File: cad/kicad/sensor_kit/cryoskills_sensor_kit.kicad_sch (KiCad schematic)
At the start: 12 parts, among them J1 PWR_SENSE_Panel, J2 PWR_SENSE_Battery, J3 PWR_In, U1 LM317_TO-220

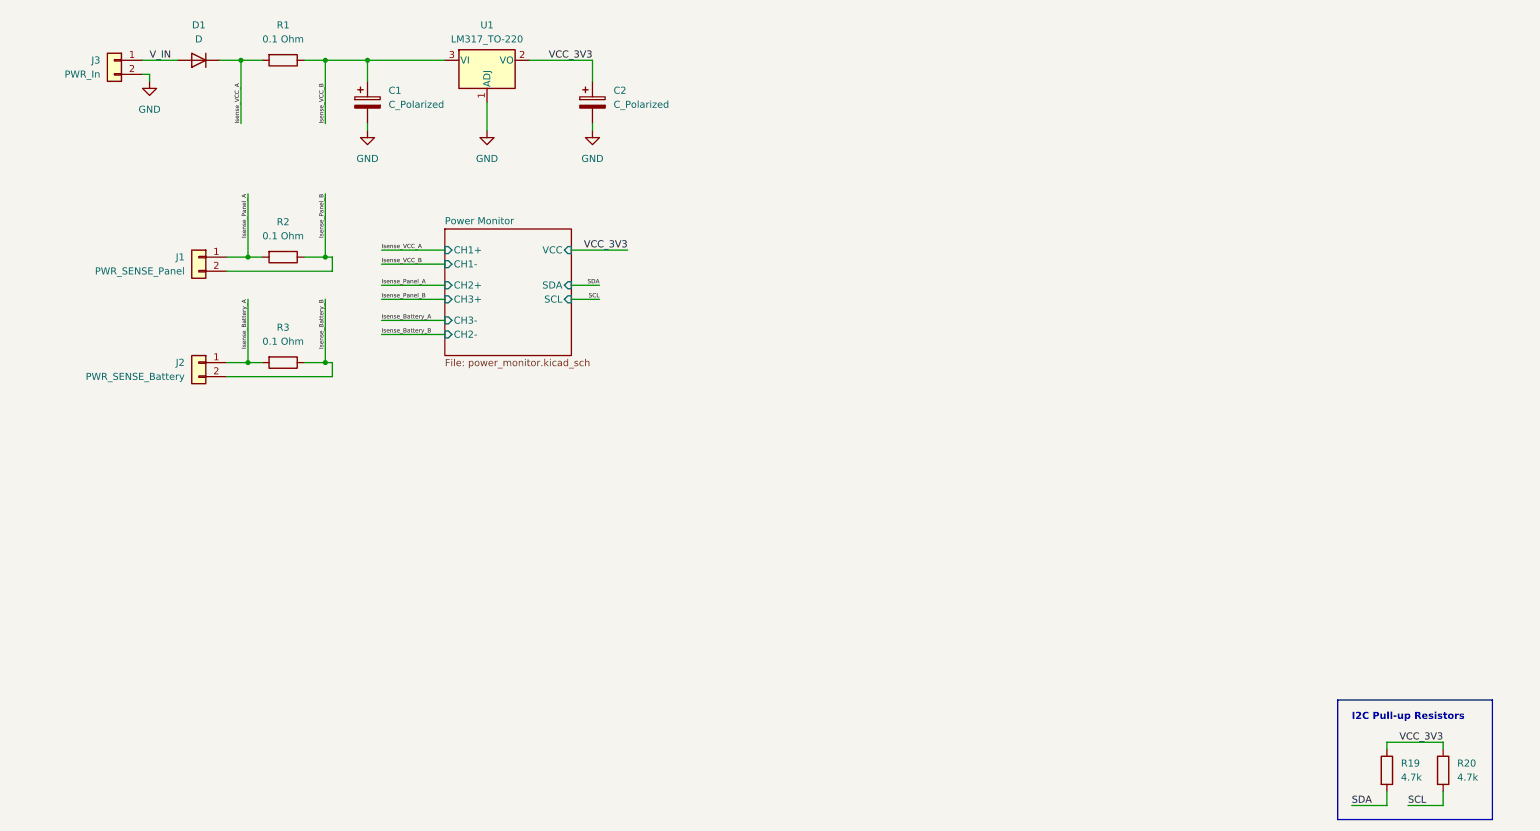
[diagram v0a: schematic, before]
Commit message: moves sensors to new board and adds discussion around ADS1120 based analog temp sensor to design notes.
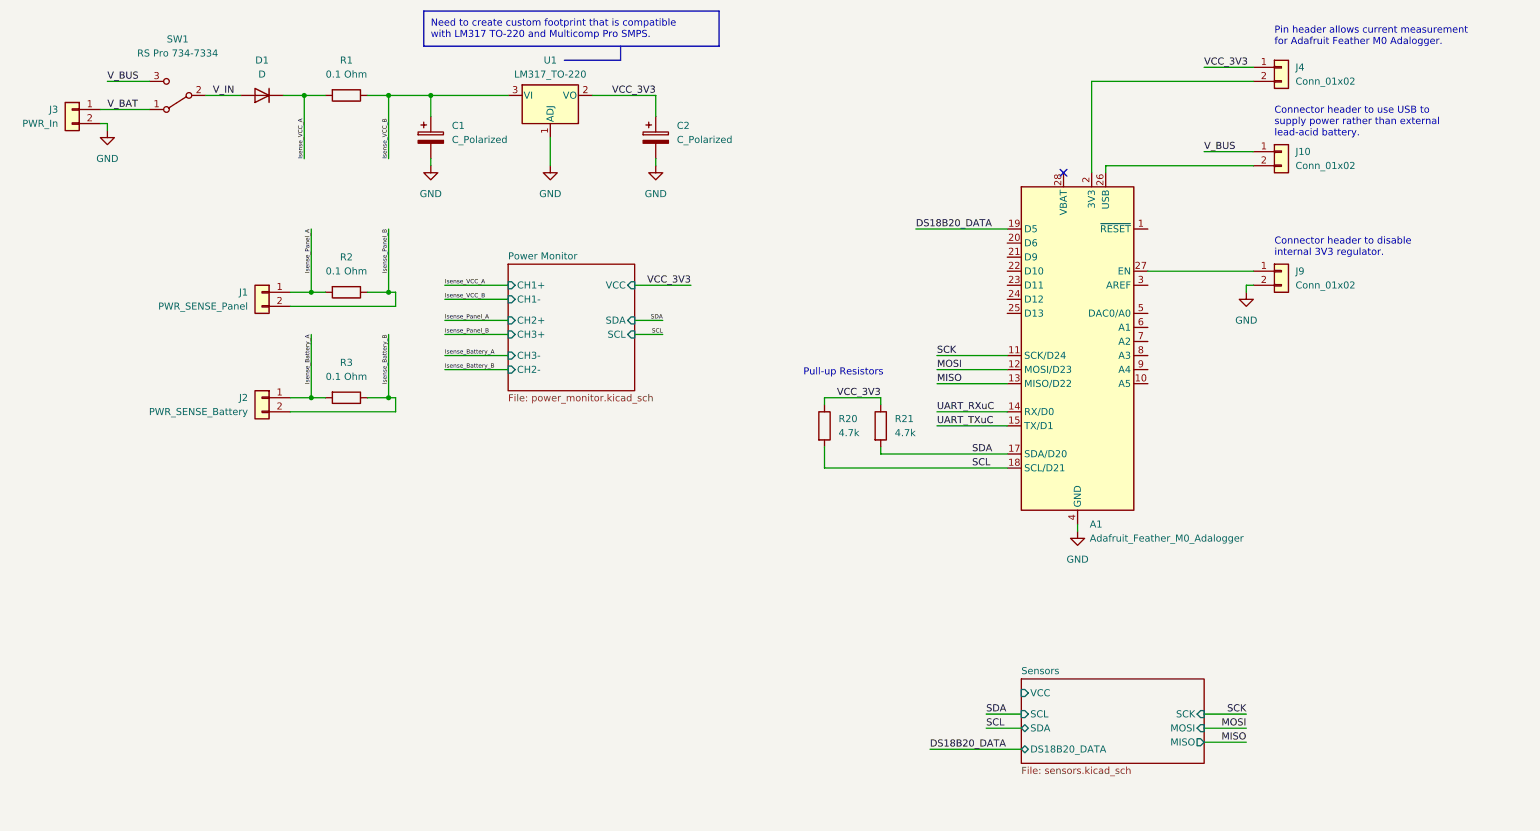
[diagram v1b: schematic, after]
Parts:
- removed R19: 4.7k, symbol Device:R
- added A1: Adafruit_Feather_M0_Adalogger, Module:Adafruit_Feather, symbol MCU_Module:Adafruit_Feather_M0_Adalogger
- added J10, J4, J9: Conn_01x02, Connector_PinHeader_2.54mm:PinHeader_1x02_P2.54mm_Vertical, symbol Connector_Generic:Conn_01x02
- added R21: 4.7k, symbol Device:R
- added SW1: RS Pro 734-7334, cryoskills_sensor_kit:RSPRO_7347334_SWSlide_SPDT, symbol Switch:SW_SPDT
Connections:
- net GND: now also A1.16 (GND), A1.4 (GND), J9.2 (Pin_2)
- net SCL: now also A1.18 (SCL/D21)
- net SDA: now also A1.17 (SDA/D20), R21.2
- net VCC_3V3: now also J4.1 (Pin_1), R21.1
- net V_IN: now also SW1.2 (B); no longer J3.1 (Pin_1)
- new net: A1.26 (USB), J10.2 (Pin_2)
- new net: A1.2 (3V3), J4.2 (Pin_2)
- new net: A1.27 (EN), J9.1 (Pin_1)
- new net DS18B20_DATA: A1.19 (D5)
- new net MISO: A1.13 (MISO/D22)
- new net MOSI: A1.12 (MOSI/D23)
- new net SCK: A1.11 (SCK/D24)
- new net UART_RXuC: A1.14 (RX/D0)
- new net UART_TXuC: A1.15 (TX/D1)
- new net V_BAT: J3.1 (Pin_1), SW1.1 (A)
- new net V_BUS: J10.1 (Pin_1), SW1.3 (C)
- no-connect marks 0 -> 1
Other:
- added sheet Sensors (sensors.kicad_sch)
- note added: "Connector header to disable internal 3V3 regulator."
- note added: "Connector header to use USB to supply power rather than external lead-acid battery."
- note added: "Need to create custom footprint that is compatible with LM317 TO-220 and Multicomp Pro SMPS."
- note added: "Pin header allows current measurement for Adafruit Feather M0 Adalogger."
- note added: "Pull-up Resistors"
- note removed: "I2C Pull-up Resistors"
- company: (none) -> Cardiff University
- title: (none) -> CryoSkills Sensor Kit
- moved on the sheet: C1, C2, D1, J1, J2, J3, R1, R2, R3, U1

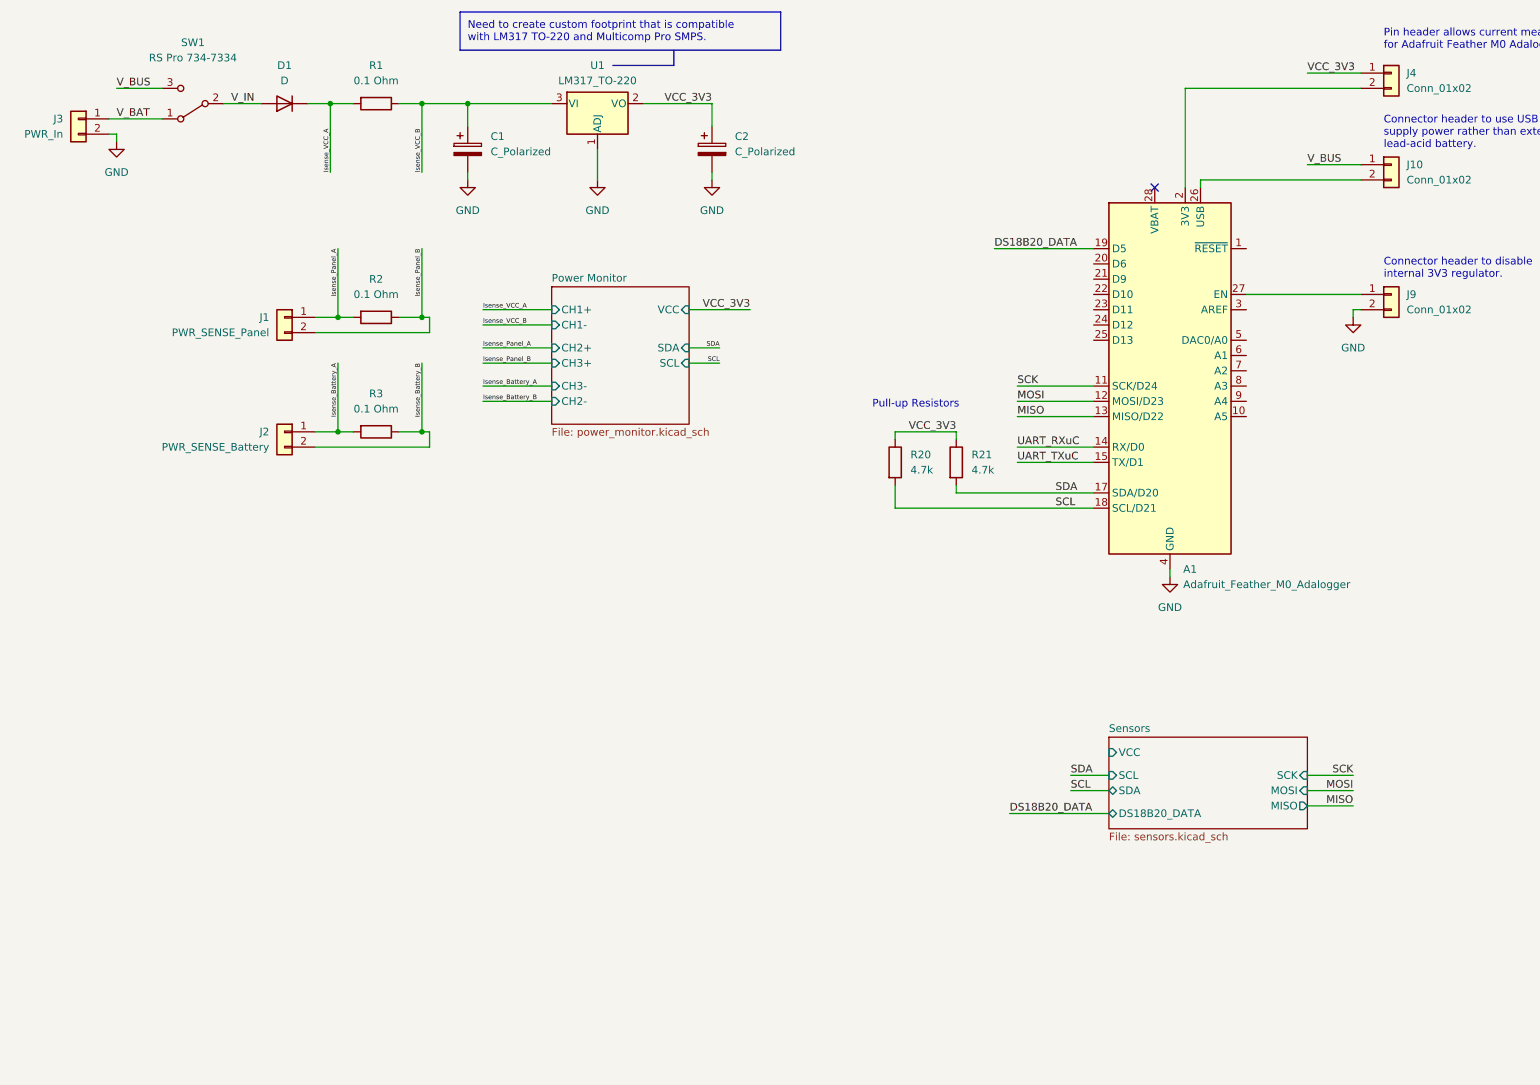
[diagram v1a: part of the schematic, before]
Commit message: adds further sensors to board layout
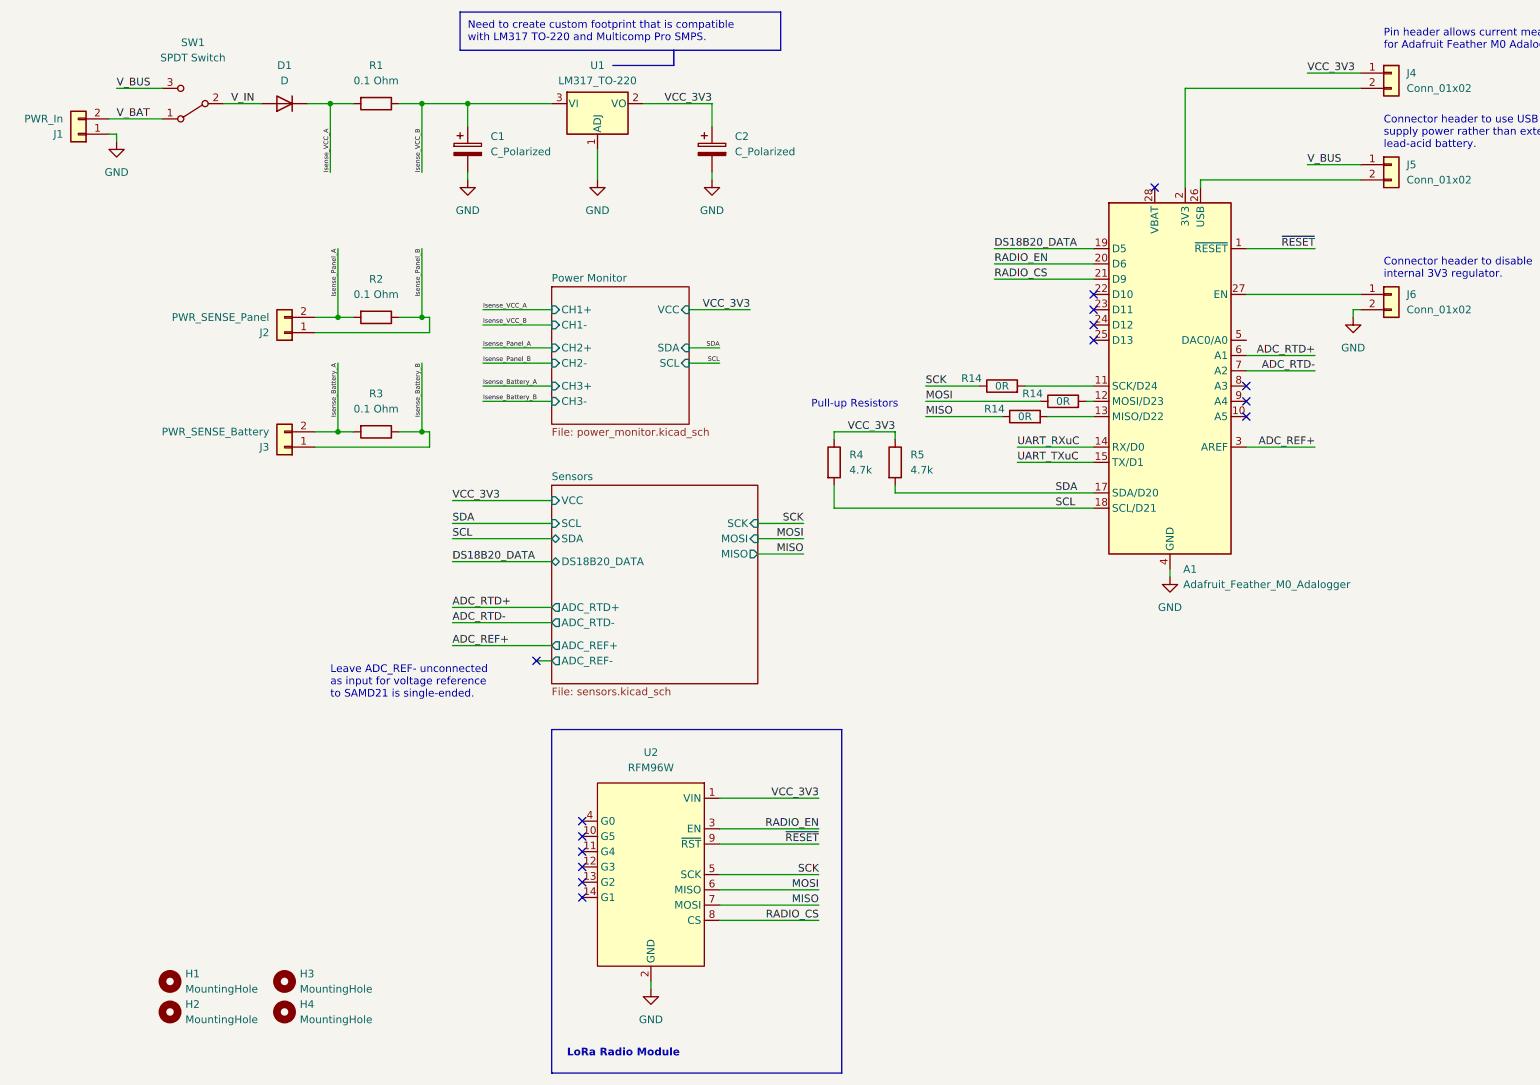
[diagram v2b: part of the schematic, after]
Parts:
- added H1, H2, H3, H4: MountingHole, MountingHole:MountingHole_3.2mm_M3, symbol Mechanical:MountingHole
- added R14 (x3): 0R, Resistor_SMD:R_0805_2012Metric_Pad1.20x1.40mm_HandSolder, symbol Device:R
- added U2: RFM96W, cryoskills_sensor_kit:RFM96W, symbol cryoskills_sensor_kit:RFM96W
- A1: Manufacturer (none) -> Adafruit; MftrPartNo (none) -> 2796; Supplier (none) -> RS Components; SupplierPartNo (none) -> 124-5517
- D1: footprint (none) -> Diode_SMD:D_SMB
- J1: renamed from J3; footprint (none) -> cryoskills_sensor_kit:TerminalBlock_Multicomp_5.08_2way_MP012059; Manufacturer (none) -> Multicomp PRO; MftrPartNo (none) -> MP12059; Supplier (none) -> Farnell; SupplierPartNo (none) -> 4179098
- J2: renamed from J1; footprint (none) -> cryoskills_sensor_kit:TerminalBlock_Multicomp_5.08_2way_MP012059; Manufacturer (none) -> Multicomp PRO; MftrPartNo (none) -> MP12059; Supplier (none) -> Farnell; SupplierPartNo (none) -> 4179098
- J3: renamed from J2; footprint (none) -> cryoskills_sensor_kit:TerminalBlock_Multicomp_5.08_2way_MP012059; Manufacturer (none) -> Multicomp PRO; MftrPartNo (none) -> MP12059; Supplier (none) -> Farnell; SupplierPartNo (none) -> 4179098
- R1, R2, R3: footprint (none) -> Resistor_SMD:R_1206_3216Metric
- R4: renamed from R20; footprint (none) -> Resistor_SMD:R_0805_2012Metric_Pad1.20x1.40mm_HandSolder
- R5: renamed from R21; footprint (none) -> Resistor_SMD:R_0805_2012Metric_Pad1.20x1.40mm_HandSolder
- SW1: value RS Pro 734-7334 -> SPDT Switch; Manufacturer (none) -> RS Pro; MftrPartNo (none) -> 734-7334; Supplier (none) -> RS Components; SupplierPartNo (none) -> 734-7334
- renumbered J10 to J5, J9 to J6
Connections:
- net GND: now also J1.1 (Pin_1), U2.2 (GND); no longer J1.2 (Pin_2)
- net Isense_Battery_A: now also J3.2 (Pin_2); no longer J3.1 (Pin_1)
- net Isense_Battery_B: now also J3.1 (Pin_1); no longer J3.2 (Pin_2)
- net Isense_Panel_A: now also J2.2 (Pin_2); no longer J2.1 (Pin_1)
- net Isense_Panel_B: now also J2.1 (Pin_1); no longer J2.2 (Pin_2)
- net MISO: now also R14.1, U2.7 (MOSI); no longer A1.13 (MISO/D22)
- net MOSI: now also R14.1, U2.6 (MISO); no longer A1.12 (MOSI/D23)
- net SCK: now also R14.1, U2.5 (SCK); no longer A1.11 (SCK/D24)
- net VCC_3V3: now also U2.1 (VIN)
- net V_BAT: now also J1.2 (Pin_2); no longer J1.1 (Pin_1)
- net ~{RESET}: now reaches A1.1 (~{RESET})
- net ~{RESET}: now also U2.9 (~{RST})
- net RADIO_EN: now reaches A1.20 (D6)
- net RADIO_EN: now also U2.3 (EN)
- net RADIO_CS: now reaches A1.21 (D9)
- net RADIO_CS: now also U2.8 (CS)
- net ADC_REF+: now reaches A1.3 (AREF)
- net ADC_RTD+: now reaches A1.6 (A1)
- net ADC_RTD-: now reaches A1.7 (A2)
- new net: A1.13 (MISO/D22), R14.2
- new net: A1.11 (SCK/D24), R14.2
- new net: A1.12 (MOSI/D23), R14.2
- no-connect marks 1 -> 15
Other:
- sheet Sensors ports: added ADC_REF+, ADC_REF-, ADC_RTD+, ADC_RTD-; removed none
- note added: "Leave ADC_REF- unconnected as input for voltage reference to SAMD21 is single-ended."
- note added: "LoRa Radio Module"
- moved on the sheet: J1, J2, J3, R4, R5

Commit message: updates sensorkit PCB with revised pinout and wheatstone bridge circuit
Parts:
- added R31: 1.2k, Resistor_SMD:R_0805_2012Metric, symbol Device:R
- added R32: 1.8k, Resistor_SMD:R_0805_2012Metric, symbol Device:R
- C1, C2: value C_Polarized -> 10uF
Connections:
- net GND: now also R32.2; no longer U1.1 (ADJ)
- net VCC_3V3: now also R31.1
- net RADIO_IRQ: now reaches U2.4 (G0)
- net RADIO_IRQ: now also A1.22 (D10)
- net RTD_WHEAT_EN: now reaches A1.23 (D11)
- new net: R31.2, R32.1, U1.1 (ADJ)
- no-connect marks 15 -> 13
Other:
- sheet Sensors ports: added RTD_WHEAT_EN; removed none
- moved on the sheet: C2

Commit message: revises sensor board to remove current source and reduce footprint
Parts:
- removed C1, C2: 10uF, symbol Device:C_Polarized
- removed R31: 1.2k, Resistor_SMD:R_0805_2012Metric, symbol Device:R
- removed R32: 1.8k, Resistor_SMD:R_0805_2012Metric, symbol Device:R
- removed U1: LM317_TO-220, Package_TO_SOT_THT:TO-220-3_Vertical, symbol Regulator_Linear:LM317_TO-220
- added C11, C12: 47pF, Resistor_SMD:R_0402_1005Metric, symbol Device:C
- added C13, C15: 100nF, Resistor_SMD:R_0402_1005Metric, symbol Device:C
- added C14: 10nF, Resistor_SMD:R_0603_1608Metric, symbol Device:C
- added C16: 4.7uF, symbol Device:C_Polarized
- added FB1: FerriteBead, Inductor_SMD:L_0603_1608Metric, symbol Device:FerriteBead
- added J10: QWIIC_I2C_2, Connector_JST:JST_SH_SM04B-SRSS-TB_1x04-1MP_P1.00mm_Horizontal, symbol Connector_Generic:Conn_01x04
- added J11: DS18B20, cryoskills_sensor_kit:TerminalBlock_Multicomp_5.08_3way_MP012060, symbol Connector_Generic:Conn_01x03
- added J12: SERIAL_BREAKOUT, Connector_PinHeader_2.54mm:PinHeader_1x04_P2.54mm_Vertical, symbol Connector_Generic:Conn_01x04
- added J13: USB_B, Connector_USB:USB_Micro-B_GCT_USB3076-30-A, symbol Connector:USB_B
- added J7: PT1000_RTD_WHEAT, cryoskills_sensor_kit:TerminalBlock_Multicomp_5.08_2way_MP012059, symbol Connector:Screw_Terminal_01x02
- added J8: SPI_BREAKOUT, Connector_PinHeader_2.54mm:PinHeader_1x04_P2.54mm_Vertical, symbol Connector_Generic:Conn_01x04
- added J9: QWIIC_I2C_1, Connector_JST:JST_SH_SM04B-SRSS-TB_1x04-1MP_P1.00mm_Horizontal, symbol Connector_Generic:Conn_01x04
- added R14 (x4): 0R, Resistor_SMD:R_0805_2012Metric_Pad1.20x1.40mm_HandSolder, symbol Device:R
- added R14 (x2): 27R, Resistor_SMD:R_0402_1005Metric, symbol Device:R
- added R24, R25: 3k3, Resistor_THT:R_Axial_DIN0204_L3.6mm_D1.6mm_P5.08mm_Horizontal, symbol Device:R
- added R26: 1k, Resistor_THT:R_Axial_DIN0204_L3.6mm_D1.6mm_P5.08mm_Horizontal, symbol Device:R
- added R27: 4.7k, Resistor_THT:R_Axial_DIN0204_L3.6mm_D1.6mm_P5.08mm_Horizontal, symbol Device:R
- added SW2: SW_Push, Button_Switch_THT:SW_PUSH_6mm, symbol Switch:SW_Push
- added U4: FT231XQ, Package_DFN_QFN:QFN-20-1EP_4x4mm_P0.5mm_EP2.5x2.5mm, symbol Interface_USB:FT231XQ
- J4: value Conn_01x02 -> Adalogger_3V3
- J5: value Conn_01x02 -> Adalogger_VBUS
- J6: value Conn_01x02 -> Adalogger_RegulatorEN
- renumbered R2 to R1, R3 to R2, R1 to R3, U2 to U1
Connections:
- net RTD_WHEAT_EN is gone; now on net ADC_REF+: A1.23 (D11)
- net ADC_REF+: now also R24.1, R25.1
- net DS18B20_DATA: now also J11.3 (Pin_3), R27.2
- net GND: now also C11.1, C12.1, C13.1, C14.2, C15.1, C16.2, J10.1 (Pin_1), J11.1 (Pin_1), J12.4 (Pin_4), J13.4 (GND), J13.5 (Shield), J7.2 (Pin_2), J8.1 (Pin_1), J9.1 (Pin_1), R26.2, SW2.2, U4.13 (GND), U4.21 (GND), U4.3 (GND)
- net Isense_VCC_A: now also SW1.2 (B); no longer D1.1 (K)
- net MISO: now also J8.4 (Pin_4)
- net MOSI: now also J8.3 (Pin_3)
- net RADIO_CS: now also A1.22 (D10); no longer A1.21 (D9)
- net RADIO_IRQ: now also A1.21 (D9); no longer A1.22 (D10)
- net SCK: now also J8.2 (Pin_2)
- net SCL: now also J10.4 (Pin_4), J9.4 (Pin_4)
- net SDA: now also J10.3 (Pin_3), J9.3 (Pin_3)
- net UART_RXuC: now also J12.2 (Pin_2), R14.2
- net UART_TXuC: now also J12.3 (Pin_3), R14.2
- net VCC_3V3: now also J10.2 (Pin_2), J11.2 (Pin_2), J12.1 (Pin_1), J9.2 (Pin_2), R27.1
- net V_BAT: now also D1.2 (A); no longer SW1.1 (A)
- net ~{RESET}: now also SW2.1
- net VBUS_Adalogger: now reaches A1.26 (USB), J5.2 (Pin_2)
- net VCC_3V3_Adalogger: now reaches A1.2 (3V3), J4.2 (Pin_2)
- net ADC_RTD+ renamed ADC_RTDp
- net ADC_RTDp: now also J7.1 (Pin_1), R24.2
- net ADC_RTD- renamed ADC_RTDm
- net ADC_RTDm: now also R25.2, R26.1
- removed net V_IN: D1.2 (A), SW1.2 (B)
- new net: C14.1, FB1.1, J13.1 (VBUS)
- new net: C15.2, C16.1, FB1.2, U4.12 (VCC)
- new net: R14.1, U4.1 (RXD)
- new net: R14.1, U4.17 (TXD)
- new net: C11.2, J13.2 (D-), R14.1
- new net: C12.2, J13.3 (D+), R14.1
- new net: C13.2, U4.10 (3V3OUT), U4.11 (~{RESET}), U4.20 (VCCIO)
- new net: R14.2, U4.8 (USBDP)
- new net: R14.2, U4.9 (USBDM)
- new net: R14.1, U4.19 (~{RTS})
- new net: R14.1, U4.6 (~{CTS})
- new net: D1.1 (K), SW1.1 (A)
- new net ~{CTS}: R14.2
- new net ~{RTS}: R14.2
- no-connect marks 13 -> 22
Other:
- removed sheet Sensors
- added sheet Voltage Regulator (voltage_regulator.kicad_sch)
- note added: "Adafruit Feather M0 Adalogger"
- note added: "Add optional LEDs for Tx/Rx data"
- note added: "DS18B20 (Digital Temp. Sensor)"
- note added: "I2C Pull-up Resistors"
- note added: "I2C QWIIC Connectors"
- note added: "Power System"
- note added: "Push to reset!"
- note added: "RTD Wheatstone Bridge"
- note added: "RTD_WH_EN is digital logic pin from Feather M0 to provide ~1mA approx"
- note added: "Radio and Serial Communications"
- note added: "SPI Breakout"
- note added: "Sensors and Peripherals"
- note added: "UART Breakout"
- note removed: "Leave ADC_REF- unconnected as input for voltage reference to SAMD21 is single-ended."
- note removed: "Need to create custom footprint that is compatible with LM317 TO-220 and Multicomp Pro SMPS."
- note removed: "Pull-up Resistors"
- moved on the sheet: A1, D1, H1, H2, H3, H4, J1, J2, J3, J4, J5, J6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
